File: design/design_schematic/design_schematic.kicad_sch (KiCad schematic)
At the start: 53 parts, among them IC1 XC9291B33D0R-G, J1 USB_C_Receptacle_USB2.0_16P, J2 Battery Pos, J3 Battery Neg, J4 OLED_128x32, J5 0781271220, U1 nRF52840, U2 BQ24072RGT, U3 USB6B1, U4 BQ27441-G1, U5 PEC11L-4015F-S0015, U6 PEC11L-4015F-S0015, X1 32MHz

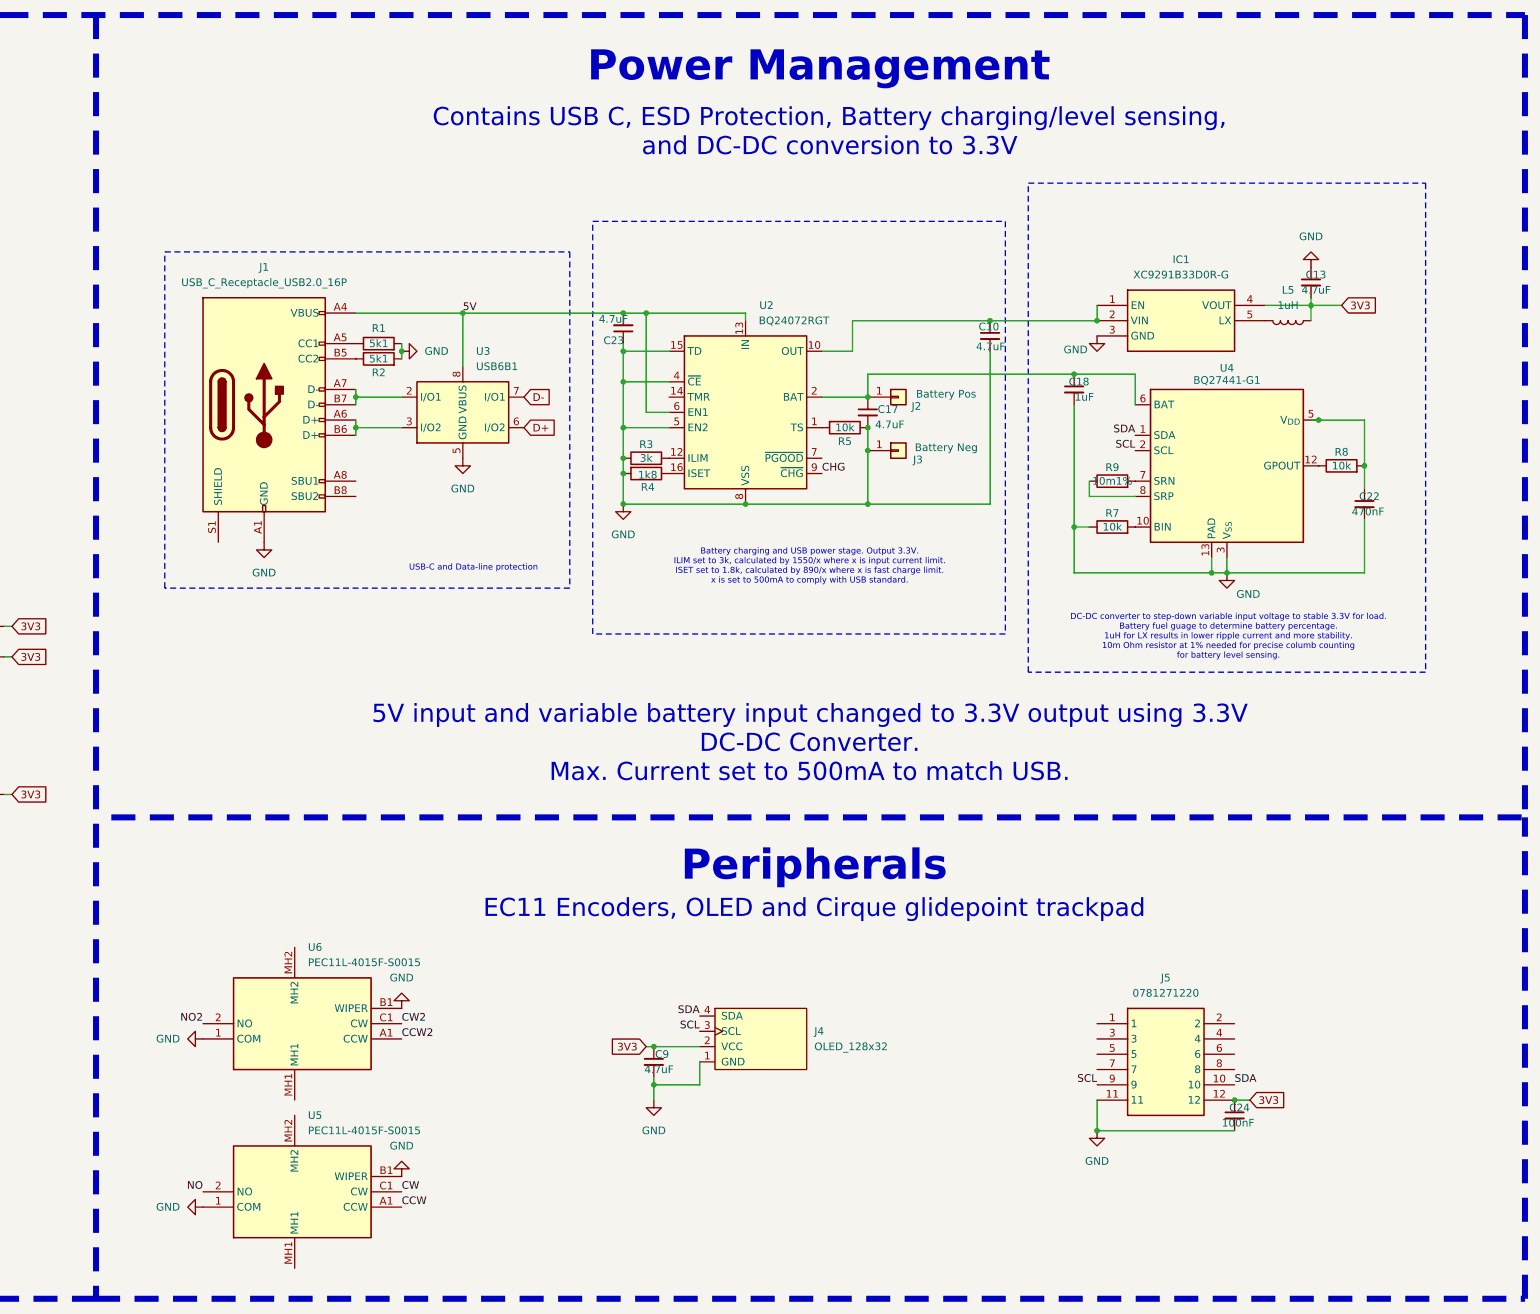
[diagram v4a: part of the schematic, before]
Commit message: add step up converter for LEDs
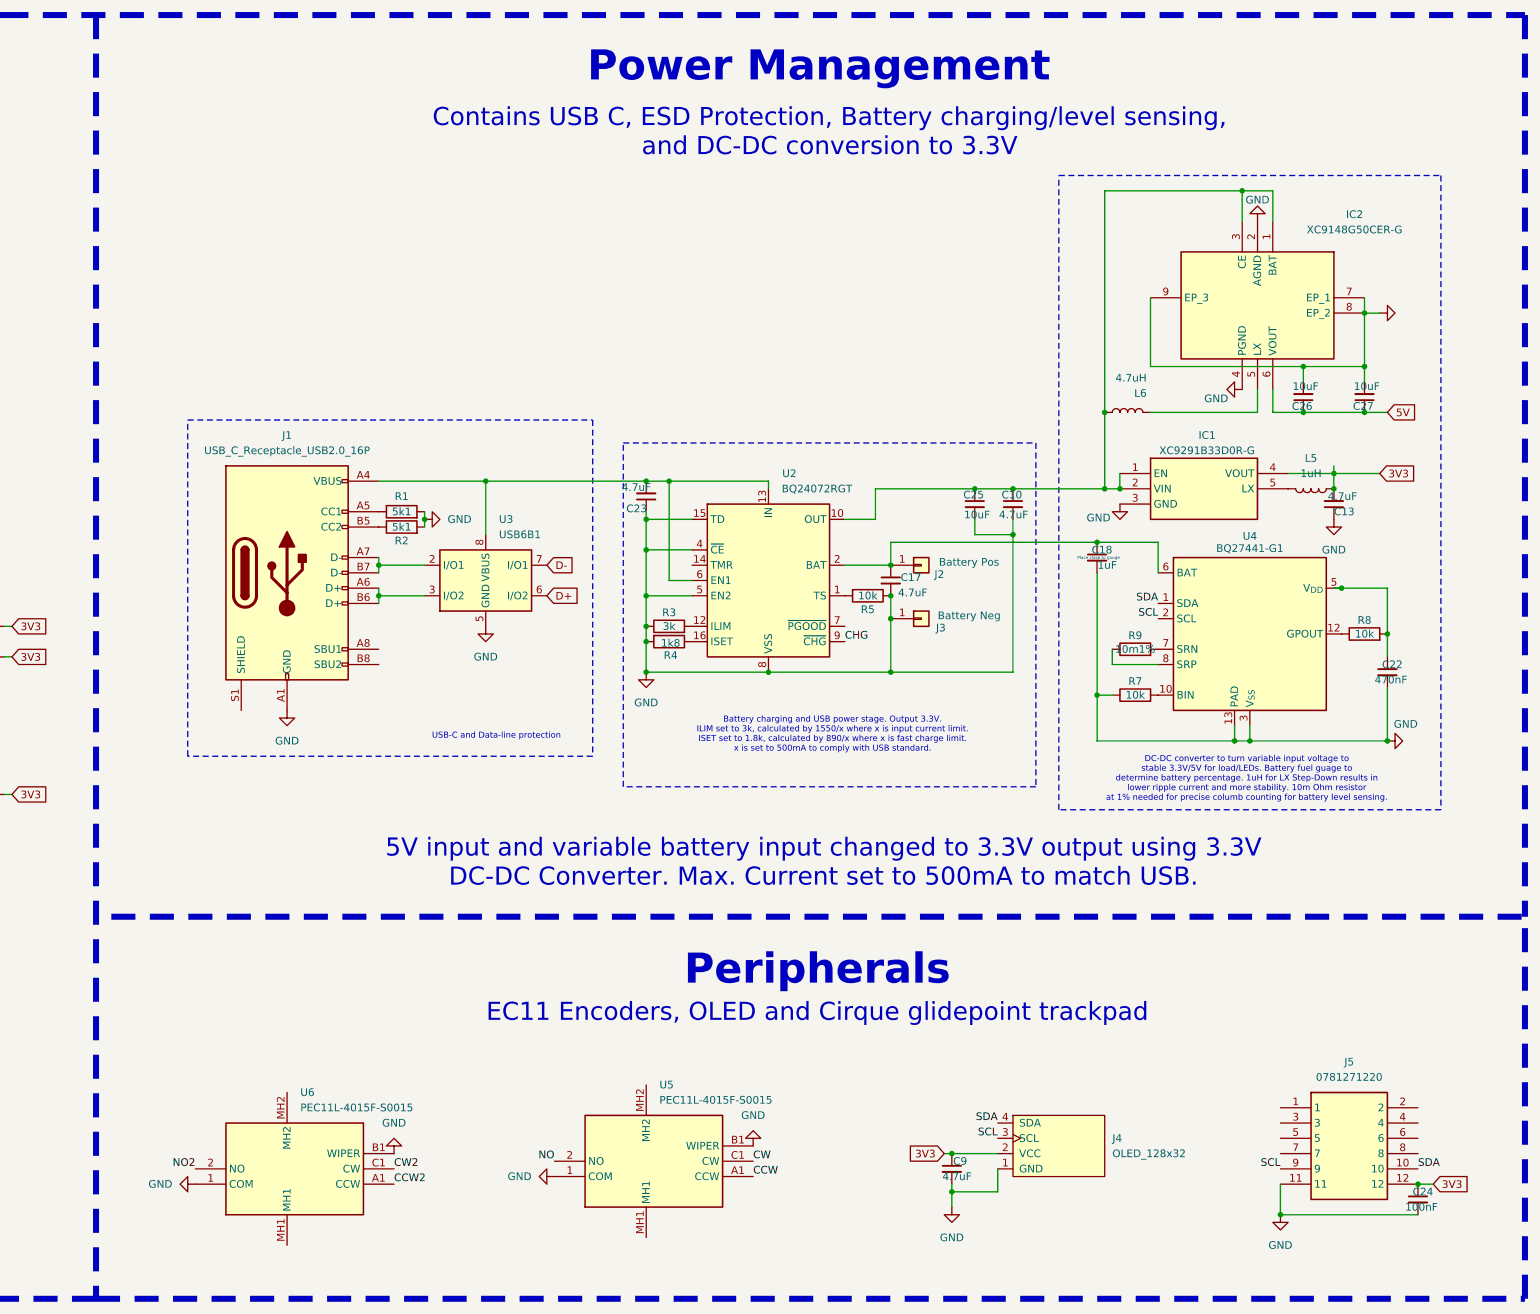
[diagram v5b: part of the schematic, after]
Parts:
- added C25, C26, C27: 10uF, ScottoKeebs_Components:Capacitor_0402, symbol Device:C_Small
- added IC2: XC9148G50CER-G, XC9147/8_USP-6C, symbol SamacSys_Parts:XC9148G50CER-G
- added L6: 4.7uH, symbol Device:L
- C18: Notes (none) -> Place close to gauge
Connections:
- net 5V: now also C26.1, C27.1, IC2.6 (VOUT); no longer C23.2, J1.A4 (VBUS), J1.A9 (VBUS), J1.B4 (VBUS), J1.B9 (VBUS), U2.13 (IN), U2.6 (EN1), U3.1 (VBUS), U3.8 (VBUS)
- net GND: now also C25.2, C26.2, C27.2, IC2.2 (AGND), IC2.4 (PGND), IC2.7 (EP_1), IC2.8 (EP_2), IC2.9 (EP_3)
- net at C10.1, IC1.1 (EN), IC1.2 (VIN)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: now also C25.1, IC2.1 (BAT), IC2.3 (CE), L6.1
- new net: C23.2, J1.A4 (VBUS), J1.A9 (VBUS), J1.B4 (VBUS), J1.B9 (VBUS), U2.13 (IN), U2.6 (EN1), U3.1 (VBUS), U3.8 (VBUS)
- new net: IC2.5 (LX), L6.2
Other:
- note added: "DC-DC converter to turn variable input voltage to stable 3.3V/5V for load/LEDs. Battery fuel guage to determine battery percentage. 1uH for LX Step-Down results in lower ripple current and more stability. 10m Ohm resistor at 1% needed for precise columb counting for battery level sensing."
- note removed: "DC-DC converter to step-down variable input voltage to stable 3.3V for load. Battery fuel guage to determine battery percentage. 1uH for LX results in lower ripple current and more stability. 10m Ohm resistor at 1% needed for precise columb counting for battery level sensing."
- moved on the sheet: C10, C17, C18, C22, C23, C24, C9, IC1, J1, J2, J3, J4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

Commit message: add LEDs
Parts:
- added C28, C31, C34, C37, C40, C43, C49: 100nF, ScottoKeebs_Components:Capacitor_0402, symbol Device:C_Small
- added C46: 10uF, ScottoKeebs_Components:Capacitor_0402, symbol Device:C_Small
- added D1, D10, D11, D12, D13, D14, D15, D16, D17, D18, D19, D2, D20, D21, D22, D23, D24, D3, D4, D5, D6, D7, D8, D9: LED_SK6812MINI, ScottoKeebs_Components:LED_SK6812MINI, symbol ScottoKeebs:LED_SK6812MINI
- added IC4: 74AHCT125PW,118, SOP65P640X110-14N, symbol SamacSys_Parts:74AHCT125PW,118
- added R12: 500, symbol Device:R
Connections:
- net 5V: now also C28.1, C31.1, C34.1, C37.1, C40.1, C43.1, C46.1, C49.1, D1.1 (VDD), D10.1 (VDD), D11.1 (VDD), D12.1 (VDD), D13.1 (VDD), D14.1 (VDD), D15.1 (VDD), D16.1 (VDD), D17.1 (VDD), D18.1 (VDD), D19.1 (VDD), D2.1 (VDD), D20.1 (VDD), D21.1 (VDD), D22.1 (VDD), D23.1 (VDD), D24.1 (VDD), D3.1 (VDD), D4.1 (VDD), D5.1 (VDD), D6.1 (VDD), D7.1 (VDD), D8.1 (VDD), D9.1 (VDD), IC4.14 (VCC)
- net GND: now also C28.2, C31.2, C34.2, C37.2, C40.2, C43.2, C46.2, C49.2, D1.3 (VSS), D10.3 (VSS), D11.3 (VSS), D12.3 (VSS), D13.3 (VSS), D14.3 (VSS), D15.3 (VSS), D16.3 (VSS), D17.3 (VSS), D18.3 (VSS), D19.3 (VSS), D2.3 (VSS), D20.3 (VSS), D21.3 (VSS), D22.3 (VSS), D23.3 (VSS), D24.3 (VSS), D3.3 (VSS), D4.3 (VSS), D5.3 (VSS), D6.3 (VSS), D7.3 (VSS), D8.3 (VSS), D9.3 (VSS), IC4.4 (2~{OE}), IC4.7 (GND)
- new net: D10.2 (DOUT), D11.4 (DIN)
- new net: D10.4 (DIN), D9.2 (DOUT)
- new net: D13.2 (DOUT), D14.4 (DIN)
- new net: D12.2 (DOUT), D13.4 (DIN)
- new net: D23.2 (DOUT), D24.4 (DIN)
- new net: D22.2 (DOUT), D23.4 (DIN)
- new net: D8.2 (DOUT), D9.4 (DIN)
- new net: D7.2 (DOUT), D8.4 (DIN)
- new net: D6.2 (DOUT), D7.4 (DIN)
- new net: D21.2 (DOUT), D22.4 (DIN)
- new net: D20.2 (DOUT), D21.4 (DIN)
- new net: D15.2 (DOUT), D16.4 (DIN)
- new net: D14.2 (DOUT), D15.4 (DIN)
- new net: D16.2 (DOUT), D17.4 (DIN)
- new net: D18.2 (DOUT), D19.4 (DIN)
- new net: D17.2 (DOUT), D18.4 (DIN)
- new net: IC4.6 (2Y), R12.1
- new net: D1.4 (DIN), R12.2
- new net: D11.2 (DOUT), D12.4 (DIN)
- new net: D1.2 (DOUT), D2.4 (DIN)
- new net: D19.2 (DOUT), D20.4 (DIN)
- new net: D3.2 (DOUT), D4.4 (DIN)
- new net: D2.2 (DOUT), D3.4 (DIN)
- new net: D5.2 (DOUT), D6.4 (DIN)
- new net: D4.2 (DOUT), D5.4 (DIN)
- new net 2A: IC4.5 (2A)
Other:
- note added: "SK6812 LEDs"
- note added: "Uses logic shifter to bring 3.3V data input to 5V, uses MOSI SPI pin for communication"

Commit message: complete schematic
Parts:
- added D25, D26, D27, D28, D29, D30, D31, D32, D33, D34, D35, D36, D37, D38, D39, D40, D41, D42, D43, D44, D45, D46, D47, D48: Diode, symbol ScottoKeebs:Placeholder_Diode
- added F1: 500mA, symbol Device:Fuse
- added J6, J7, J8, J9: Conn_01x01, symbol Connector_Generic:Conn_01x01
- added R13: 10k, symbol Device:R
- added S1, S10, S11, S12, S13, S14, S15, S16, S17, S18, S19, S2, S20, S21, S22, S23, S24, S3, S4, S5, S6, S7, S8, S9: Keyswitch, symbol ScottoKeebs:Placeholder_Keyswitch
- added SW1: SW_SPST, symbol Switch:SW_SPST
- added SW2: SW_Push, symbol Switch:SW_Push
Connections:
- net 2A: now also U1.AC21 (P0.25)
- net 3V3: now also J8.1 (Pin_1), R13.1
- net GND: now also J1.S1 (SHIELD), J9.1 (Pin_1), SW2.2
- net Column 0: now reaches U1.A12 (AIN0/P0.02)
- net Column 0: now also S1.1, S2.1, S3.1, S4.1
- net at U1.AA24 (SWDCLK): now also J6.1 (Pin_1)
- net at U1.AC13 (P0.18/~{RESET}): now also R13.2, SW2.1
- net at U1.AC24 (SWDIO): now also J7.1 (Pin_1)
- net Column 1: now reaches U1.B13 (AIN1/P0.03)
- net Column 1: now also S5.1, S6.1, S7.1, S8.1
- net Column 2: now reaches U1.J1 (AIN2/P0.04)
- net Column 2: now also S10.1, S11.1, S12.1, S9.1
- net Column 3: now reaches U1.K2 (AIN3/P0.05)
- net Column 3: now also S13.1, S14.1, S15.1, S16.1
- net Column 4: now reaches U1.L1 (P0.06)
- net Column 4: now also S17.1, S18.1, S19.1, S20.1
- net Column 5: now reaches U1.N1 (P0.08)
- net Column 5: now also S21.1, S22.1, S23.1, S24.1
- net Row 3: now reaches U1.P23 (P1.07)
- net Row 3: now also D28.1 (K), D32.1 (K), D36.1 (K), D40.1 (K), D44.1 (K), D48.1 (K)
- net Row 2: now reaches U1.R24 (P1.06)
- net Row 2: now also D27.1 (K), D31.1 (K), D35.1 (K), D39.1 (K), D43.1 (K), D47.1 (K)
- net Row 1: now reaches U1.T23 (P1.05)
- net Row 1: now also D26.1 (K), D30.1 (K), D34.1 (K), D38.1 (K), D42.1 (K), D46.1 (K)
- net Row 0: now reaches U1.U24 (P1.04)
- net Row 0: now also D25.1 (K), D29.1 (K), D33.1 (K), D37.1 (K), D41.1 (K), D45.1 (K)
- net at C23.2, U2.13 (IN), U2.6 (EN1)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: now also F1.2; no longer J1.A4 (VBUS), J1.A9 (VBUS), J1.B4 (VBUS), J1.B9 (VBUS)
- net at C10.1, C25.1, IC1.1 (EN)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: now also SW1.2 (B); no longer U2.10 (OUT), U2.11 (OUT)
- new net: D34.2 (A), S10.2
- new net: D27.2 (A), S3.2
- new net: D33.2 (A), S9.2
- new net: D28.2 (A), S4.2
- new net: D45.2 (A), S21.2
- new net: D30.2 (A), S6.2
- new net: D32.2 (A), S8.2
- new net: D29.2 (A), S5.2
- new net: D26.2 (A), S2.2
- new net: D42.2 (A), S18.2
- new net: D43.2 (A), S19.2
- new net: D48.2 (A), S24.2
- new net: D25.2 (A), S1.2
- new net: D36.2 (A), S12.2
- new net: F1.1, J1.A4 (VBUS), J1.A9 (VBUS), J1.B4 (VBUS), J1.B9 (VBUS)
- new net: D41.2 (A), S17.2
- new net: D39.2 (A), S15.2
- new net: SW1.1 (A), U2.10 (OUT), U2.11 (OUT)
- new net: D31.2 (A), S7.2
- new net: D37.2 (A), S13.2
- new net: D40.2 (A), S16.2
- new net: D46.2 (A), S22.2
- new net: D44.2 (A), S20.2
- new net: D38.2 (A), S14.2
- new net: D47.2 (A), S23.2
- new net: D35.2 (A), S11.2
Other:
- note added: "Switches"

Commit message: pcb place switches, leds, diodes and stabiliser right side
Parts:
- removed D26, D27, D28, D30, D31, D32, D34, D35, D36, D38, D39, D40, D42, D43, D44, D46, D47, D48: Diode, symbol ScottoKeebs:Placeholder_Diode
- removed J6, J7, J8, J9: Conn_01x01, symbol Connector_Generic:Conn_01x01
- added Di10, Di11, Di12, Di13, Di14, Di15, Di16, Di17, Di18, Di19, Di20, Di21, Di22, Di23, Di24, Di7, Di8, Di9: Diode, ScottoKeebs_Components:Diode_SOD-123, symbol ScottoKeebs:Placeholder_Diode
- added J6: Conn_01x05, symbol Connector_Generic:Conn_01x05
- Di1: renamed from D25; footprint (none) -> ScottoKeebs_Components:Diode_SOD-123
- Di2: renamed from D29; footprint (none) -> ScottoKeebs_Components:Diode_SOD-123
- Di3: renamed from D33; footprint (none) -> ScottoKeebs_Components:Diode_SOD-123
- Di4: renamed from D37; footprint (none) -> ScottoKeebs_Components:Diode_SOD-123
- Di5: renamed from D41; footprint (none) -> ScottoKeebs_Components:Diode_SOD-123
- Di6: renamed from D45; footprint (none) -> ScottoKeebs_Components:Diode_SOD-123
- IC1: footprint XC9290A07E0RG -> SamacSys_Parts:XC9290A07E0RG
- IC2: footprint XC9147/8_USP-6C -> (none)
- IC4: footprint SOP65P640X110-14N -> SamacSys_Parts:SOP65P640X110-14N
- J5: footprint 0781271220 -> SamacSys_Parts:0781271220
- S1, S10, S11, S12, S13, S14, S15, S16, S17, S18, S19, S2, S20, S21, S22, S23, S24, S3, S4, S5, S6, S7, S8, S9: footprint (none) -> ScottoKeebs_Hotswap:Hotswap_Choc_V1_1.00u
- U5, U6: footprint PEC11L4015FS0015 -> SamacSys_Parts:PEC11L4015FS0015
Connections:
- net 3V3: now also J6.2 (Pin_2)
- net Column 0: now also S10.1, S18.1; no longer S3.1, S4.1
- net Column 1: now also S11.1, S19.1, S3.1; no longer S6.1, S7.1, S8.1
- net Column 2: now also S20.1, S4.1; no longer S10.1, S11.1
- net Column 3: now also S22.1, S6.1; no longer S15.1, S16.1
- net Column 4: now also S15.1, S23.1, S7.1; no longer S18.1, S19.1, S20.1
- net Column 5: now also S16.1, S8.1; no longer S22.1, S23.1
- net GND: now also J6.3 (Pin_3)
- net Row 1: now also Di10.1 (K), Di11.1 (K), Di12.1 (K), Di7.1 (K), Di8.1 (K), Di9.1 (K)
- net Row 2: now also Di13.1 (K), Di14.1 (K), Di15.1 (K), Di16.1 (K), Di17.1 (K), Di18.1 (K)
- net Row 3: now also Di19.1 (K), Di20.1 (K), Di21.1 (K), Di22.1 (K), Di23.1 (K), Di24.1 (K)
- net at S10.2: now also Di13.2 (A)
- net at S3.2: now also Di8.2 (A)
- net at S4.2: now also Di9.2 (A)
- net at S6.2: now also Di10.2 (A)
- net at S8.2: now also Di12.2 (A)
- net at S2.2: now also Di7.2 (A)
- net at S18.2: now also Di19.2 (A)
- net at U1.AA24 (SWDCLK): now also J6.4 (Pin_4)
- net at R13.2, SW2.1, U1.AC13 (P0.18/~{RESET}): now also J6.1 (Pin_1)
- net at U1.AC24 (SWDIO): now also J6.5 (Pin_5)
- net at S19.2: now also Di20.2 (A)
- net at S24.2: now also Di24.2 (A)
- net at S12.2: now also Di15.2 (A)
- net at S15.2: now also Di17.2 (A)
- net at S7.2: now also Di11.2 (A)
- net at S16.2: now also Di18.2 (A)
- net at S22.2: now also Di22.2 (A)
- net at S20.2: now also Di21.2 (A)
- net at S14.2: now also Di16.2 (A)
- net at S23.2: now also Di23.2 (A)
- net at S11.2: now also Di14.2 (A)
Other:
- moved on the sheet: C12, C14, C17, C22, C23, C6, C8, J2, J3, R1, R2, R3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
